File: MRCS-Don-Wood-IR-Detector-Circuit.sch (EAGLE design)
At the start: 20 parts, among them U1 LM324N

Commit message: first board sent to JLC
first board
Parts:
- removed BOARD1: BOARD80X100, SPCoast:BOARD80X100
- removed FID1, FID2: FIDUCIAL, SPCoast:FIDUCIAL
- removed OSHW1: DOC-OSHW-LOGO-M, SPCoast:DOC-OSHW-LOGO-M
- added CON1: DC PWR, SPCoast:CONNECTOR-DC-POWER-RA
- added LED1, LED2: RED, SPCoast:LEDLED3MM
- added R11: 0, SPCoast:RPTH-R0
- added R12: 470, SPCoast:RPTH04
- R8: value 0 -> 470; device SPCoast:RPTH-R0 -> SPCoast:RPTH04
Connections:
- net N$1 renamed REF1
- net N$14 renamed A2
- net N$3 renamed B2
- net N$4 renamed A1
- net N$6 renamed IN1
- net N$7 renamed IN2
- net N$8 renamed REF2
- removed net N$5: J1.3, R8.2
- new net B1: J1.3, R11.2
- new net N$1: LED2.C, R12.2
- new net N$16: LED1.C, R8.2
- net +5V: now also CON1.1
- net GND: now also CON1.2, CON1.3, J3.A, J4.A, R12.1, R8.1; no longer J3.B, J4.B
- net N$11: now also LED2.A
- net N$13: now also LED1.A, R11.1; no longer R8.1
- net VCC: now also J3.B, J4.B; no longer J3.A, J4.A
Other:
- note added: "Test LED"
- moved on the sheet: R6, R8

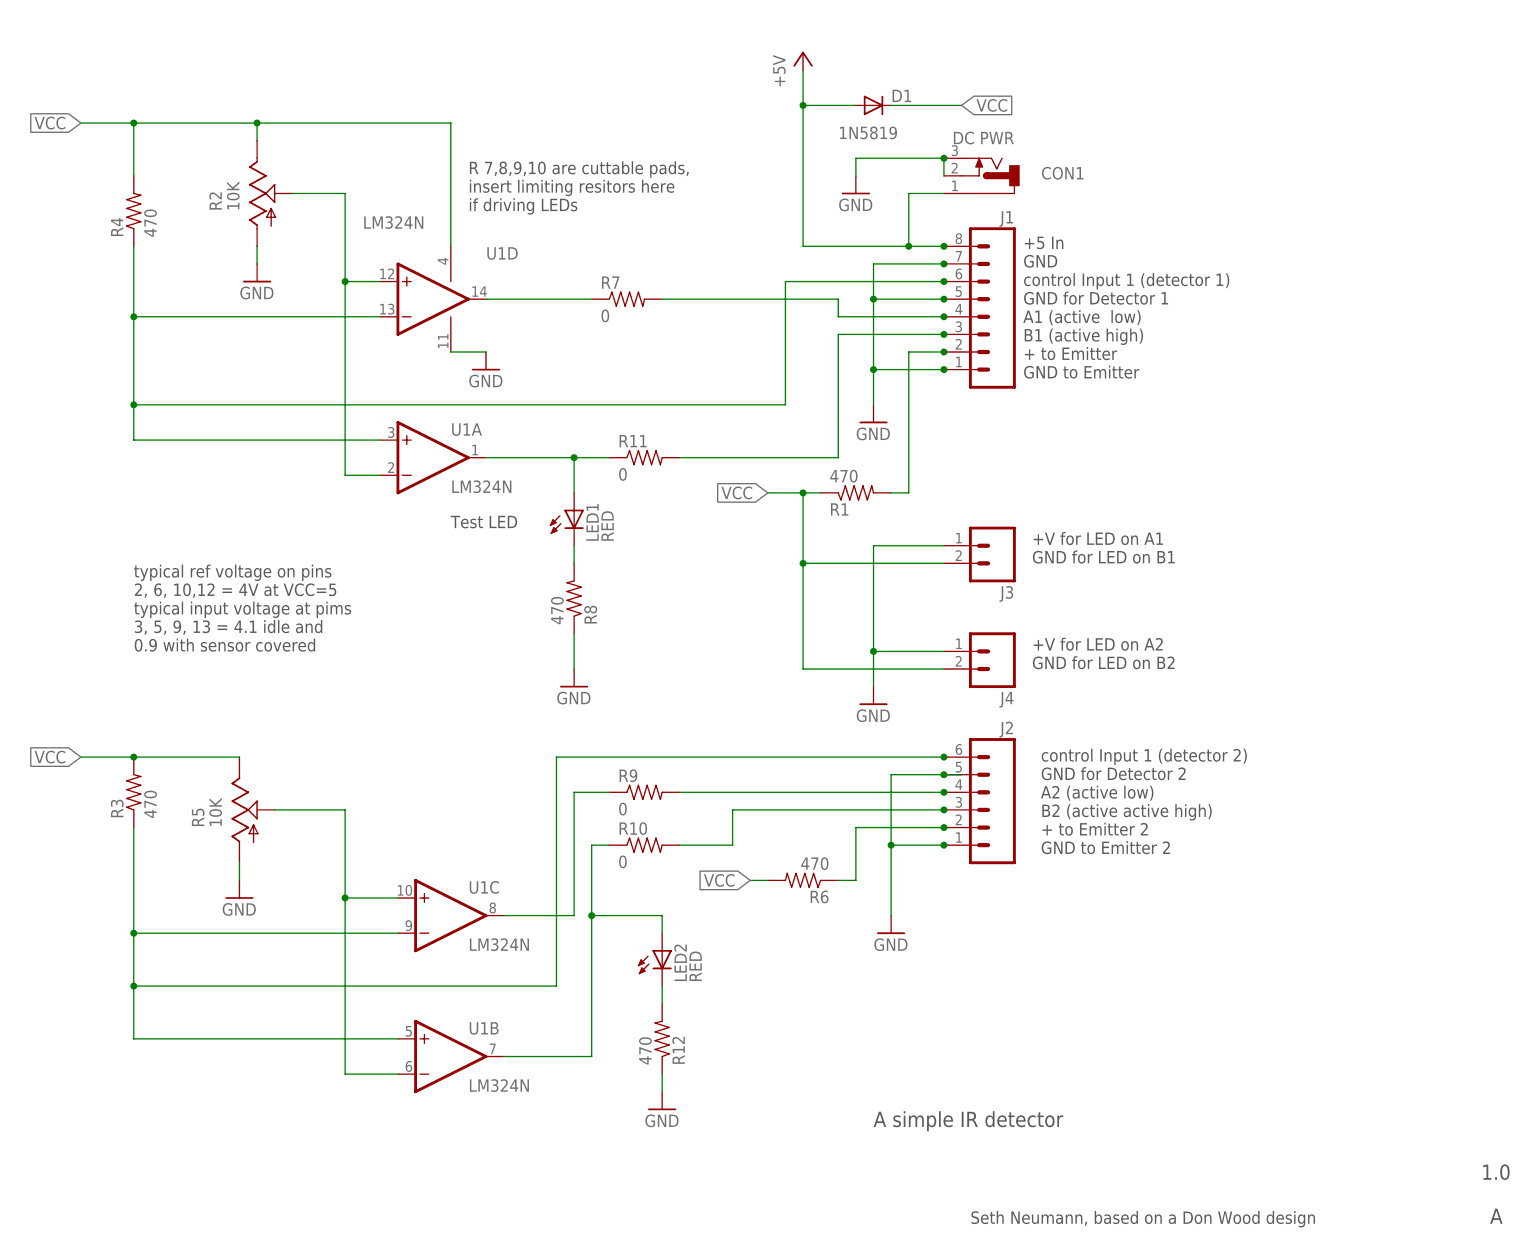
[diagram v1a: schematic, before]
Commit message: moved the status LED to show illumination present
The LED now lights when the the illumination is present.  This is to help calibrate detection when using InfraRed illumination and reflected light set ups.
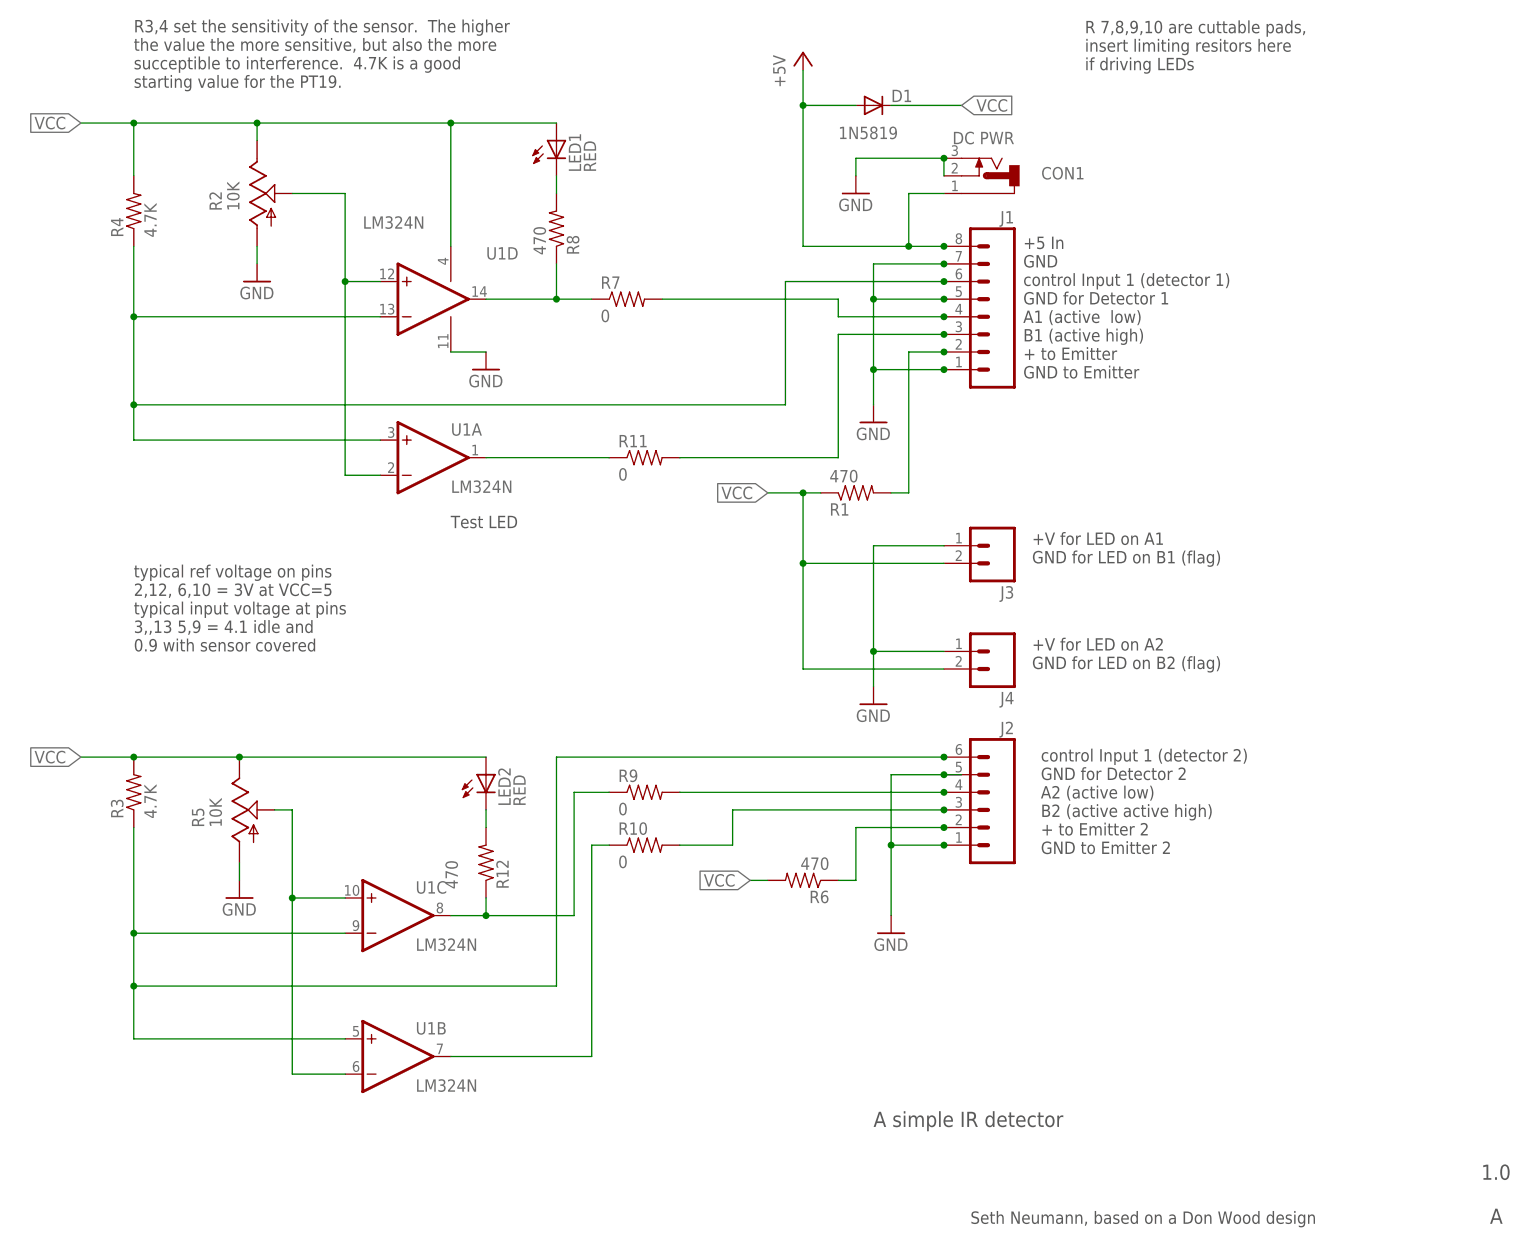
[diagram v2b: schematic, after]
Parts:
- R3, R4: value 470 -> 4.7K
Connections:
- net GND: no longer R12.1, R8.1
- net N$10: now also R12.1
- net N$11: no longer LED2.A
- net N$13: no longer LED1.A
- net N$9: now also R8.1
- net VCC: now also LED1.A, LED2.A
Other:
- note added: "+V for LED on A1 GND for LED on B1 (flag)"
- note added: "+V for LED on A2 GND for LED on B2 (flag)"
- note added: "R3,4 set the sensitivity of the sensor. The higher the value the more sensitive, but also the more succeptible to interference. 4.7K is a good starting value for the PT19."
- note added: "typical ref voltage on pins 2,12, 6,10 = 3V at VCC=5 typical input voltage at pins 3,,13 5,9 = 4.1 idle and 0.9 with sensor covered"
- note removed: "+V for LED on A1 GND for LED on B1"
- note removed: "+V for LED on A2 GND for LED on B2"
- note removed: "typical ref voltage on pins 2, 6, 10,12 = 4V at VCC=5 typical input voltage at pims 3, 5, 9, 13 = 4.1 idle and 0.9 with sensor covered"
- moved on the sheet: LED1, LED2, R12, R8, U1B, U1C
